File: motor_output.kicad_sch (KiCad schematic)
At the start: 11 parts

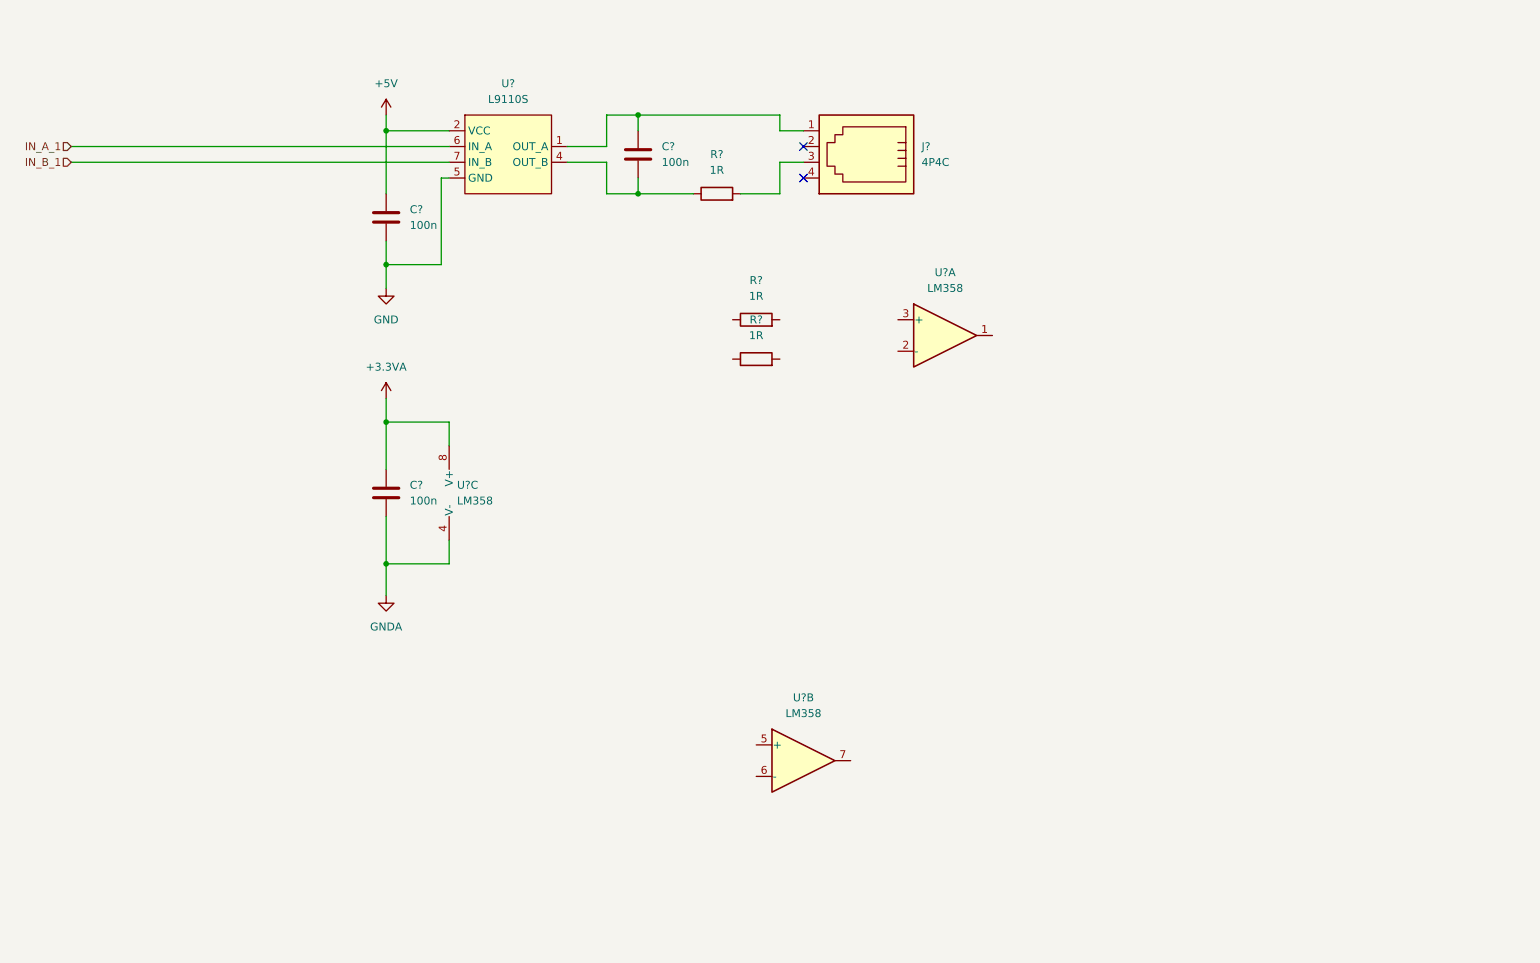
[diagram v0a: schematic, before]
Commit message: changed gain of opamps
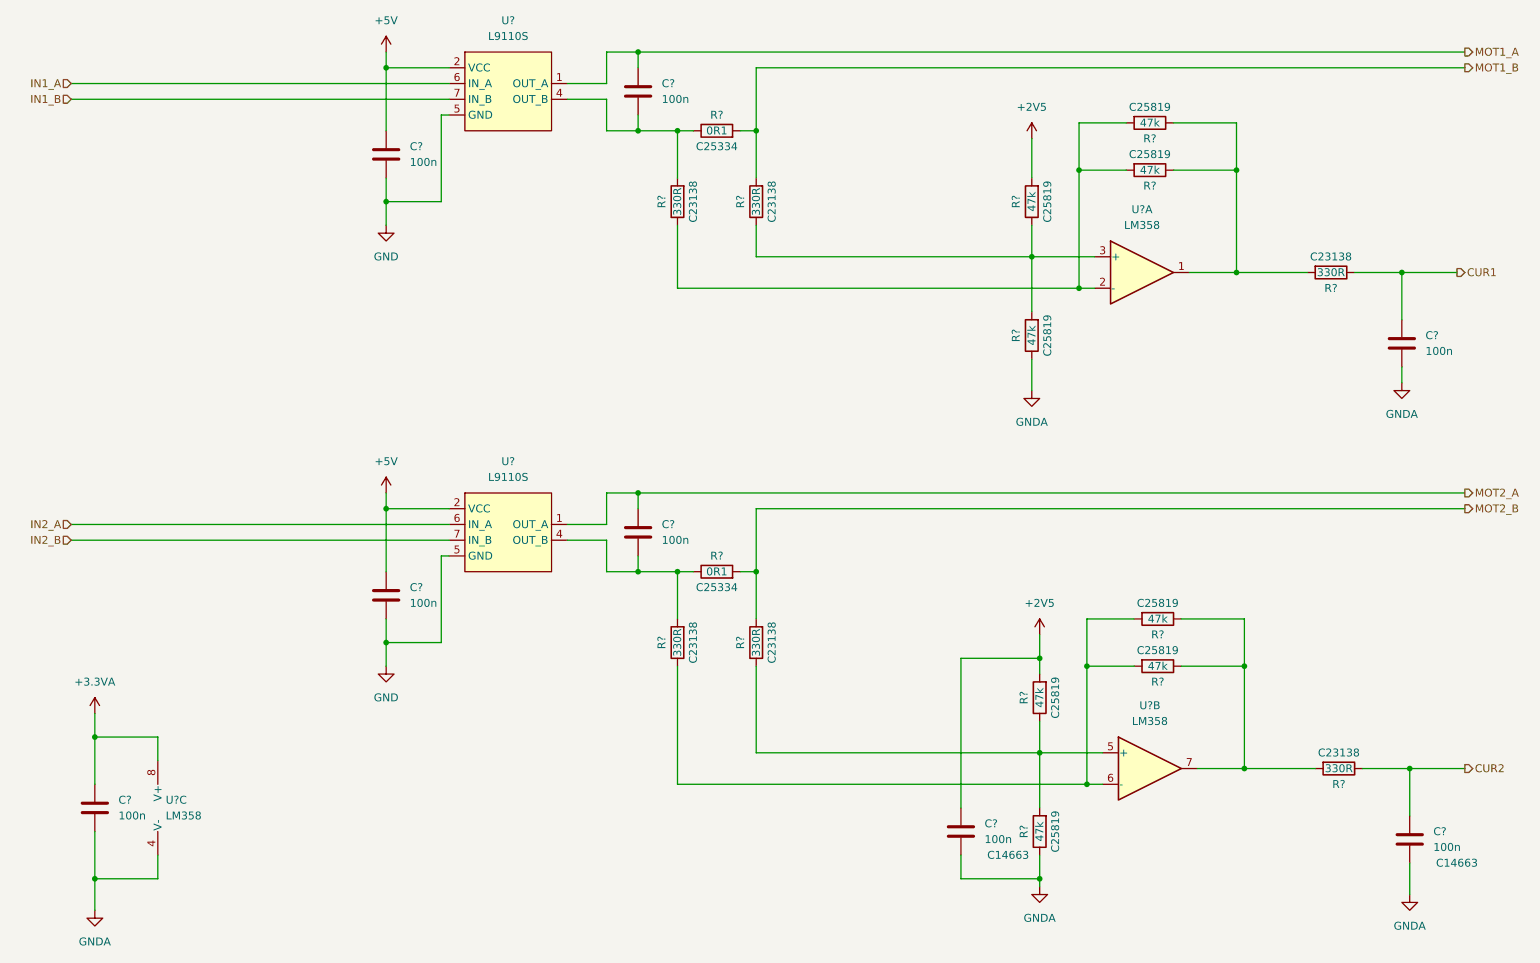
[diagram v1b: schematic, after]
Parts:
- removed J?: 4P4C, symbol Connector:4P4C
- removed R? (x2): 1R, symbol Device:R
- added C? (x5): 100n, Capacitor_SMD:C_0603_1608Metric, symbol Device:C
- added R?: 0R1, Resistor_SMD:R_1206_3216Metric, symbol Device:R
- added R? (x8): 47k, Resistor_SMD:R_0603_1608Metric, symbol Device:R
- added R? (x6): 330R, Resistor_SMD:R_0603_1608Metric, symbol Device:R
- added U?: L9110S, Package_SO:SO-8_3.9x4.9mm_P1.27mm, symbol L9110S:L9110S
- C? (x2): JLCPCB (none) -> C14663
- C?: footprint (none) -> Capacitor_SMD:C_0603_1608Metric; JLCPCB (none) -> C14663
- R?: value 1R -> 0R1; footprint (none) -> Resistor_SMD:R_1206_3216Metric; JLCPCB (none) -> C25334
- U?: JLCPCB (none) -> C513306
- U? (x3): JLCPCB (none) -> C351426
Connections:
- net +5V: now also C?.1, U?.2 (VCC), U?.3 (VCC)
- net GND: now also C?.2, U?.5 (GND), U?.8 (GND)
- net GNDA: now also C?.2, C?.2, C?.2, R?.1, R?.1
- net MOT1_A: now reaches C?.1, U?.1 (OUT_A)
- net at C?.2, R?.1, U?.4 (OUT_B): now also R?.2
- net MOT1_B: now reaches R?.2
- net MOT1_B: now also R?.2
- net at U?.1: now also R?.1, R?.1, R?.2
- net at U?.2 (-): now also R?.1, R?.2, R?.2
- net at U?.3 (+): now also R?.1, R?.1, R?.2
- net at U?.5 (+): now also R?.1, R?.1, R?.2
- net at U?.6 (-): now also R?.1, R?.2, R?.2
- net at U?.7: now also R?.1, R?.1, R?.2
- net IN_A_1 renamed IN1_A
- net IN_B_1 renamed IN1_B
- new net: C?.2, R?.1, R?.2, U?.4 (OUT_B)
- new net +2V5: C?.1, R?.2, R?.2
- new net CUR1: C?.1, R?.1
- new net CUR2: C?.1, R?.1
- new net IN2_A: U?.6 (IN_A)
- new net IN2_B: U?.7 (IN_B)
- new net MOT2_A: C?.1, U?.1 (OUT_A)
- new net MOT2_B: R?.2, R?.2
- no-connect marks 2 -> 0
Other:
- moved on the sheet: C?, R?, U?, U?A, U?B, U?C

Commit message: finished schematics
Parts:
- removed C?: 100n, Capacitor_SMD:C_0603_1608Metric, symbol Device:C
- added C9: 1n, Capacitor_SMD:C_0603_1608Metric, symbol Device:C
- C8: renamed from C?; value 100n -> 1n; JLCPCB C14663 -> C1588
- U3: renamed from U?; footprint (none) -> Package_SO:SO-8_3.9x4.9mm_P1.27mm
- gave numbers to parts that had none: 24
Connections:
- net GNDA is gone; now on net GND: C2.2, C7.2, C8.2, R10.1, R12.1, U3.4 (V-)
- net CUR2: now also C9.1
- net GND: now also C9.2
- net +3.3VA renamed +3V3
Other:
- moved on the sheet: C6

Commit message: first placing
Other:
- title: (none) -> Floor Heating Controller S2
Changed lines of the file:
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@@
 (kicad_sch (version 20211123) (generator eeschema)
   (paper "A4")
+  (title_block
+    (title "Floor Heating Controller S2")
+    (date "2022-11-30")
+    (rev "1")
+  )
   (junction (at 223.52 41.91) (diameter 0) (color 0 0 0 0)
   )
